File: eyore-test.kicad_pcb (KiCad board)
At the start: 2 copper layers, 50 x 50 mm, 29 parts, among them P1 USB_5PIN_SHELL, P2 CONN_01X04, P3 CONN_01X02, SW1 SW_PUSHBUTTON, SW2 SW_PUSHBUTTON, U1 LD1117S33CTR, U2 STM32F072C8, U3 ESP-12E, U4 ESP-12E

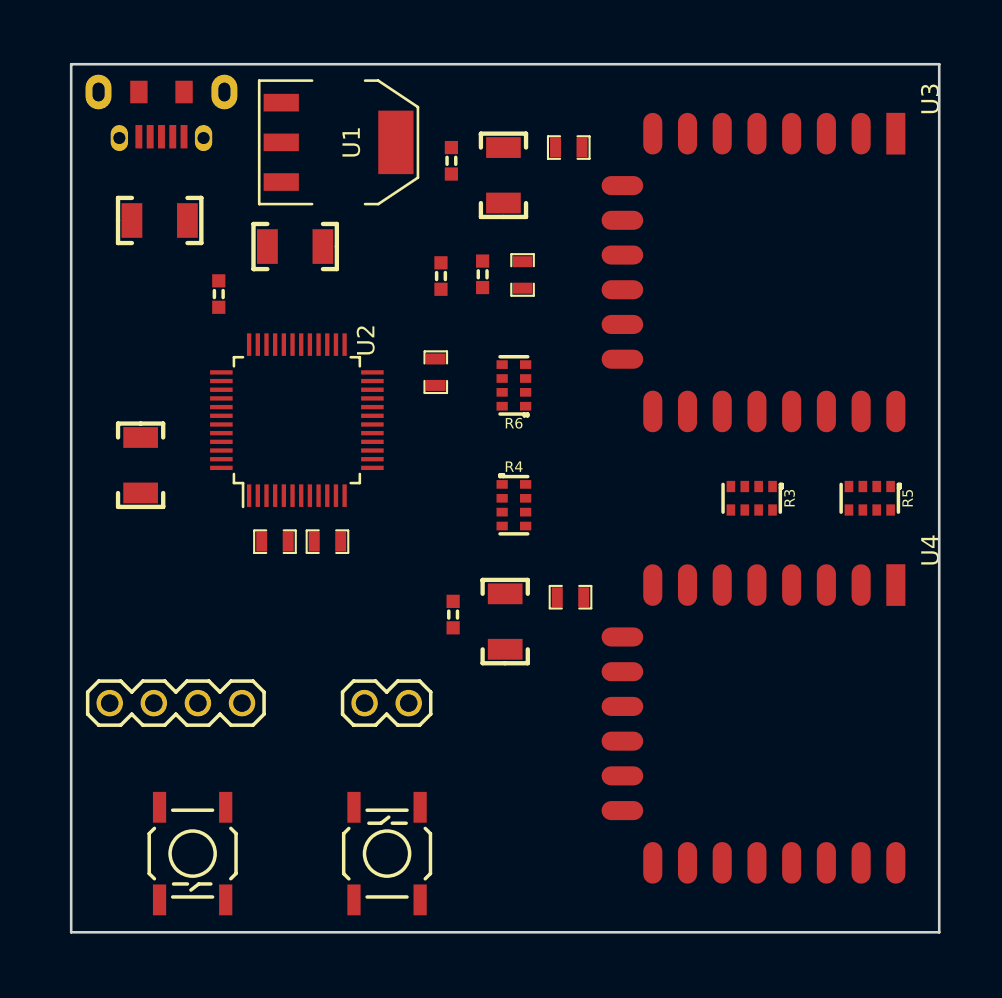
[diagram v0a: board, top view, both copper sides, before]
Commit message: Part routed, but I think approach was wrong
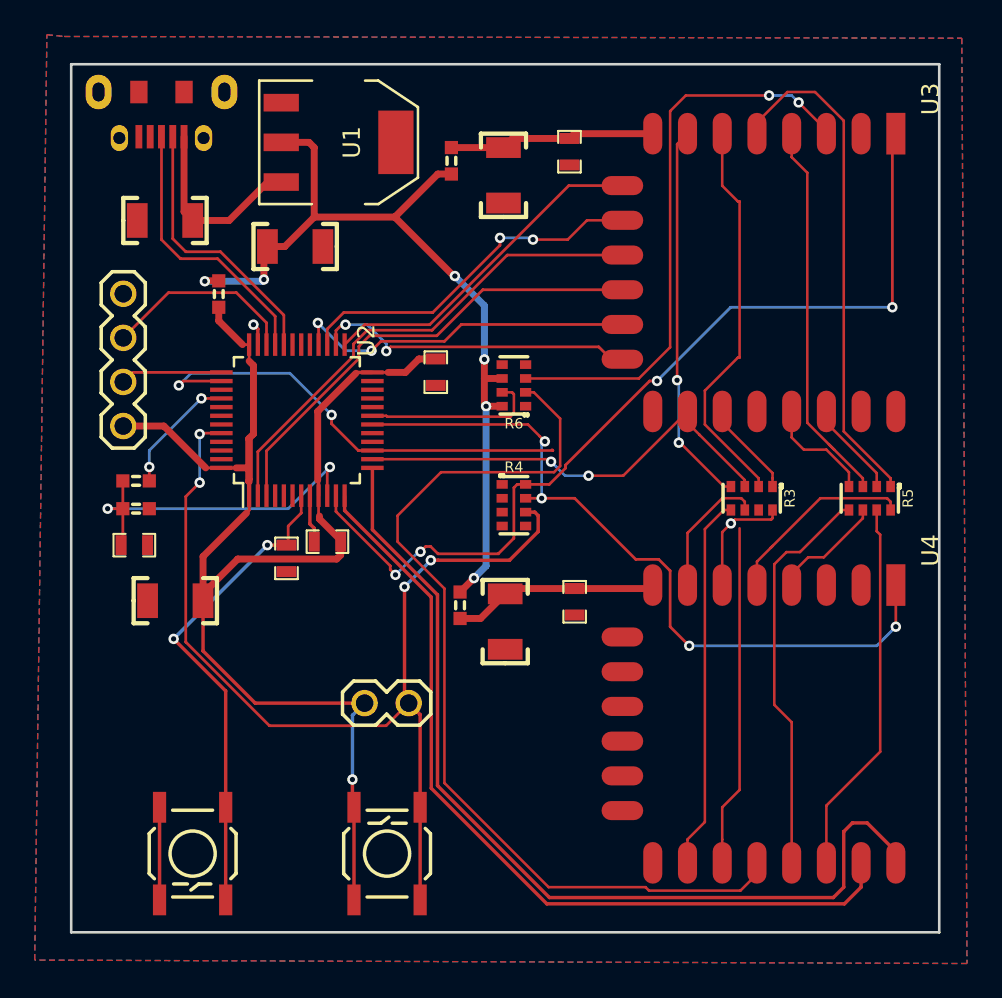
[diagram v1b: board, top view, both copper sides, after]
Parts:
- moved C4 27.2 mm to (116.6, 97.7), turned to 0 degrees
- moved R2 24.1 mm to (116.7, 95.6), turned to 180 degrees
- moved R1 21.2 mm to (116.7, 94.0), turned to 0 degrees
- moved P2 17.4 mm to (116.0, 90.8), turned to 90 degrees
- moved C5 8.05 mm to (119.0, 100.9), turned to 180 degrees
- moved C3 1.17 mm to (125.4, 98.5), turned to 270 degrees
- moved L3 0.67 mm to (135.4, 101.2), turned to 270 degrees
- moved C11 0.35 mm to (142.0, 101.0), turned to 270 degrees
- moved C1 0.30 mm to (118.4, 79.0)
- moved C10 0.24 mm to (141.7, 75.0), turned to 270 degrees
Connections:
- P2 pad 1: +3V3 -> /STM_VCC
- P3 pad 1: +3V3 -> /STM_VCC
- R3 pad 1: /A_GPIO16 -> /A_GPIO2
- R3 pad 2: /B_GPIO16 -> /B_GPIO2
- R3 pad 3: /A_GPIO14 -> /A_GPIO12
- R3 pad 4: /B_GPIO14 -> /B_GPIO12
- R3 pad 5: /A_GPIO12 -> /A_GPIO15
- R3 pad 6: /B_GPIO12 -> /B_GPIO13
- R3 pad 7: /A_GPIO2 -> /A_GPIO13
- R3 pad 8: /B_GPIO2 -> /B_GPIO15
- R5 pad 1: /A_GPIO13 -> /A_GPIO14
- R5 pad 2: /B_GPIO13 -> /B_GPIO14
- R5 pad 3: /A_GPIO15 -> /A_GPIO5_SDA
- R5 pad 4: /B_GPIO15 -> /B_GPIO5
- R5 pad 5: /A_GPIO5_SDA -> /A_GPIO16
- R5 pad 6: /B_GPIO5 -> /B_GPIO16
- SW1 pad 1: +3V3 -> /STM_VCC
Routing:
- net /STM_VCC: track 0.00 -> 85.7 mm, vias 0 -> 1
- net /STM_BOOT: track 0.00 -> 58.1 mm, vias 0 -> 4
- net /A_GPIO14: track 0.00 -> 55.9 mm, vias 0 -> 2
- net /B_GPIO0: track 0.00 -> 54.0 mm
- net /B_UART_TX: track 0.00 -> 53.9 mm
- net /A_~RST: track 0.00 -> 53.2 mm, vias 0 -> 4
- net +3V3: track 0.00 -> 51.1 mm, vias 0 -> 6
- net /B_UART_RX: track 0.00 -> 48.2 mm
- net /B_~RST: track 0.00 -> 43.3 mm, vias 0 -> 4
- net /A_ENABLE: track 0.00 -> 33.1 mm, vias 0 -> 2
- net /A_SPI_GPIO9: track 0.00 -> 28.6 mm
- net /STM_~RST: track 0.00 -> 28.0 mm, vias 0 -> 2
- net /A_SPI_GPIO10: track 0.00 -> 27.3 mm
- net /A_GPIO15: track 0.00 -> 25.8 mm, vias 0 -> 2
- net /B_GPIO4: track 0.00 -> 23.2 mm
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- added copper zone on B.Cu, net GND
- added copper zone on F.Cu, net GND
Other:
- net class Default: clearance 0.2 -> 0.15; trace_width 0.25 -> 0.15; via_drill 0.4 -> 0.3
- net class Power added: clearance 0.2, trace_width 0.25, via_dia 0.6, via_drill 0.3
- rule trace_clearance: 0.2 -> 0.15
- rule trace_min: 0.2 -> 0.15

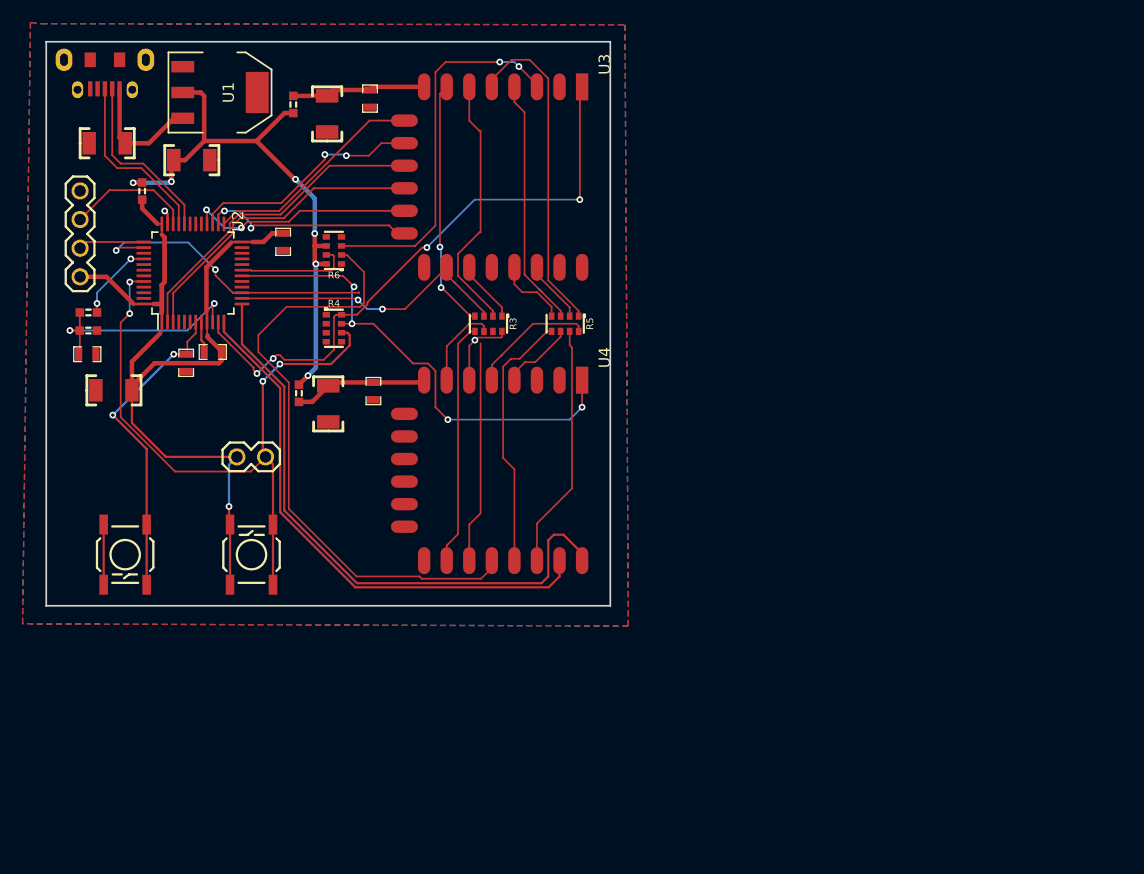
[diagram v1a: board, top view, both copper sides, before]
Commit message: Routed 4 layer version
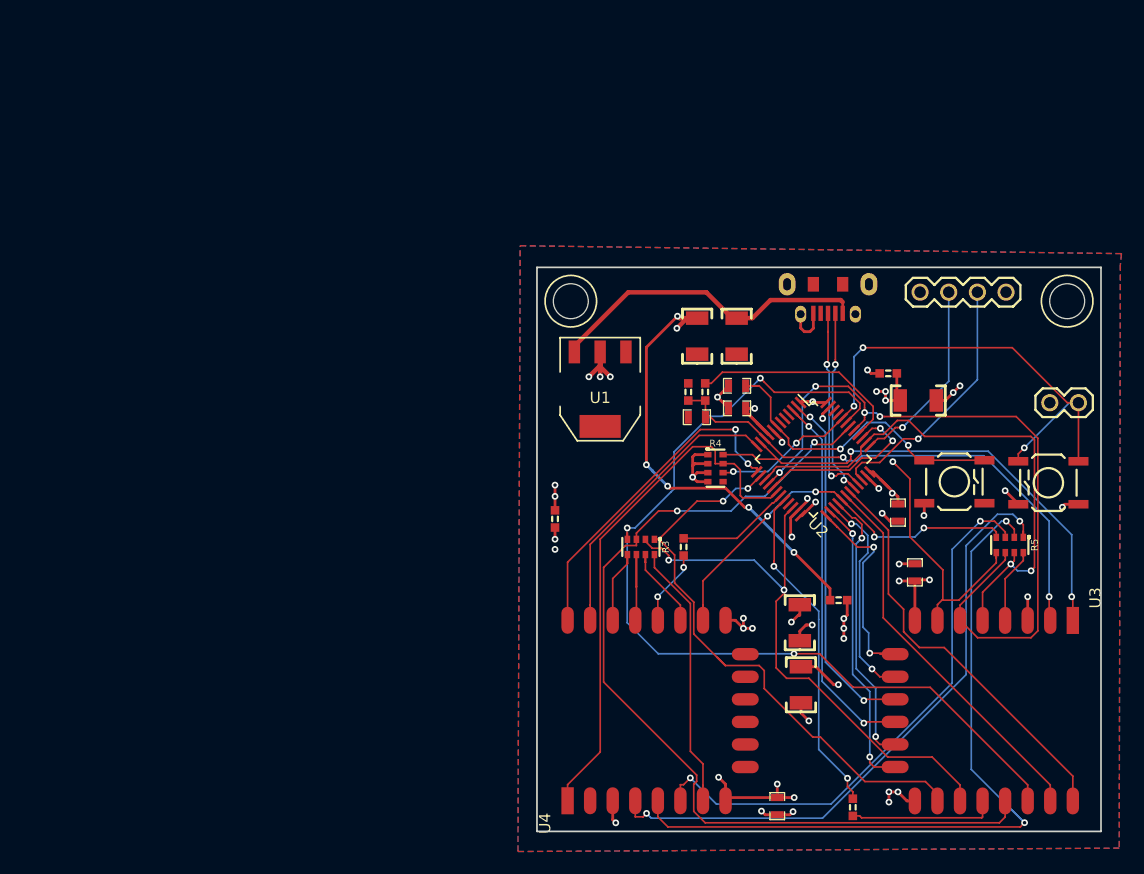
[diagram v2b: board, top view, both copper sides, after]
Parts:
- added 1pin: VAL**, Connect:1pin, F.Cu at (203.5, 93.0)
- added 1pin: VAL**, Connect:1pin, F.Cu at (159.5, 93.0)
- added R7: 10K, FT:0603, F.Cu at (184.5, 137.9)
- R6: value 220R -> 10K; footprint FT:RES_CAY16 -> FT:0603
- moved P2 74.5 mm to (190.5, 92.2), turned to 0 degrees
- moved SW2 73.8 mm to (193.5, 109.0), turned to 0 degrees
- moved P3 72.2 mm to (202.0, 102.0)
- moved C5 71.3 mm to (190.3, 101.8), turned to 0 degrees
- moved SW1 70.9 mm to (201.8, 109.1), turned to 180 degrees
- moved L1 68.1 mm to (187.6, 99.4), turned to 0 degrees
- moved P1 67.1 mm to (182.3, 94.1)
- moved C8 65.8 mm to (179.9, 127.0)
- moved L2 65.3 mm to (183.2, 119.5), turned to 0 degrees
- moved U3 64.3 mm to (204.0, 121.3)
- moved C10 64.0 mm to (190.0, 117.0), turned to 90 degrees
- moved C7 62.4 mm to (188.5, 111.7), turned to 270 degrees
- moved C1 58.4 mm to (174.2, 96.1), turned to 270 degrees
- moved U2 57.4 mm to (181.0, 107.0), turned to 315 degrees
- moved R1 55.1 mm to (171.4, 101.0), turned to 90 degrees
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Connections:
- R3 pad 1: /A_GPIO2 -> /A_GPIO15
- R3 pad 2: /B_GPIO2 -> /B_GPIO13
- R3 pad 3: /A_GPIO12 -> /A_GPIO2
- R3 pad 4: /B_GPIO12 -> /B_GPIO2
- R3 pad 5: /A_GPIO15 -> /A_GPIO4_SCL
- R3 pad 6: /B_GPIO13 -> /B_GPIO4
- R3 pad 7: /A_GPIO13 -> /A_GPIO5_SDA
- R3 pad 8: /B_GPIO15 -> /B_GPIO5
- R5 pad 1: /A_GPIO14 -> /B_GPIO16
- R5 pad 2: /B_GPIO14 -> /A_GPIO16
- R5 pad 3: /A_GPIO5_SDA -> /B_GPIO14
- R5 pad 4: /B_GPIO5 -> /A_GPIO14
- R5 pad 5: /A_GPIO16 -> /B_GPIO12
- R5 pad 6: /B_GPIO16 -> /A_GPIO12
- R5 pad 7: /A_GPIO4_SCL -> /B_GPIO15
- R5 pad 8: /B_GPIO4 -> /A_GPIO13
- R6 pad 1: /B_ENABLE -> /B_~FLASH
- R6 pad 2: +3V3 -> /B_GPIO0
- U3 pad 3: /A_ENABLE -> /A_VCC
- U4 pad 3: /B_ENABLE -> /B_VCC
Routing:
- net /A_GPIO5_SDA: track 6.48 -> 84.0 mm, vias 0 -> 3
- net /A_GPIO4_SCL: track 6.45 -> 83.8 mm, vias 0 -> 2
- net /B_GPIO14: track 11.3 -> 68.9 mm, vias 0 -> 2
- net /STM_VCC: track 85.7 -> 33.9 mm, vias 1 -> 9
- net /B_GPIO16: track 6.55 -> 56.0 mm, vias 0 -> 2
- net /B_GPIO0: track 54.0 -> 7.35 mm, vias 0 -> 2
- net /A_GPIO2: track 5.52 -> 51.6 mm, vias 0 -> 2
- net /B_GPIO12: track 4.29 -> 49.6 mm, vias 1 -> 2
- net /A_GPIO12: track 23.0 -> 67.3 mm, vias 0 -> 4
- net /A_UART_TX: track 0.00 -> 36.9 mm
- net GND: track 9.34 -> 43.9 mm, vias 1 -> 22
- net /A_UART_RX: track 0.00 -> 34.5 mm
- net /A_ENABLE: track 33.1 -> 0.00 mm, vias 2 -> 0
- net /A_~FLASH: track 0.00 -> 31.0 mm, vias 0 -> 2
- net /A_AIN: track 20.1 -> 46.5 mm
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- added copper zone on VCC, net +3V3
- added copper zone on VCC, net /A_VCC
- added copper zone on VCC, net /B_VCC
- added copper zone on VCC, net /STM_VCC
- added copper zone on Gnd, net GND
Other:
- copper layers 2 -> 4

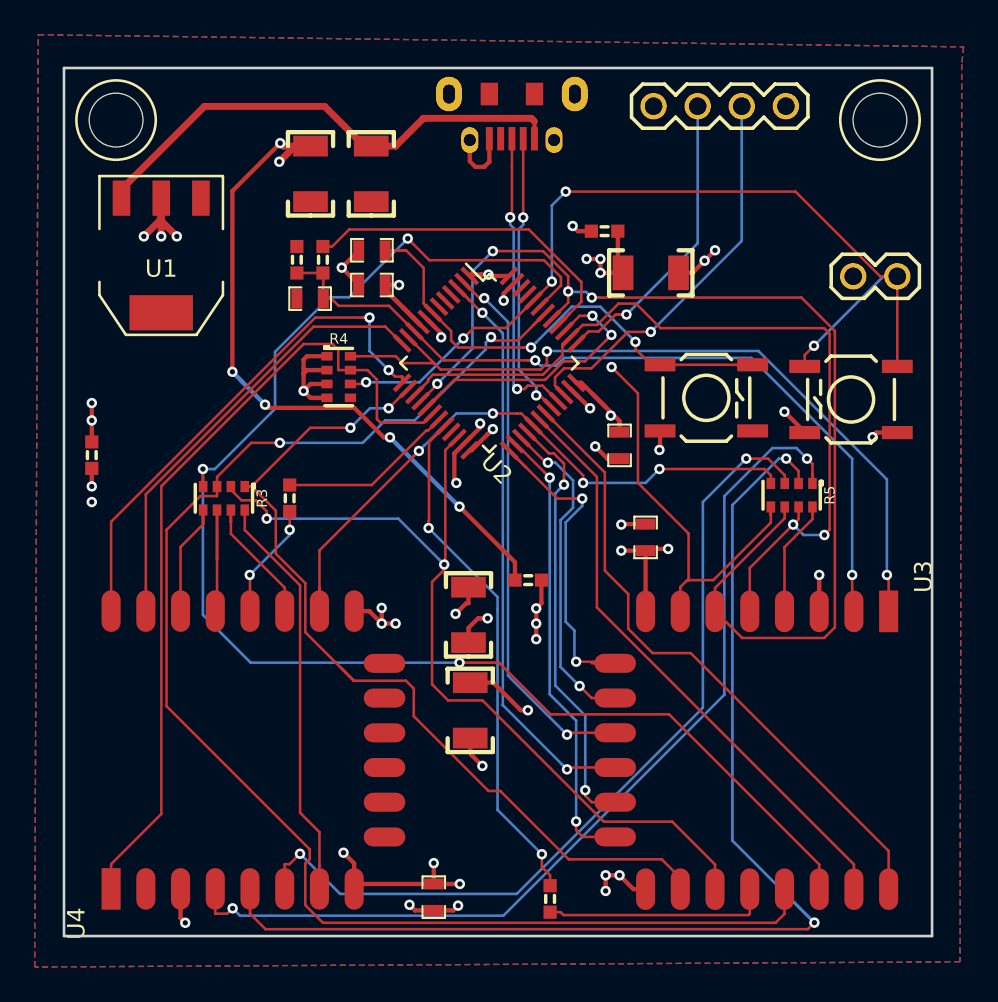
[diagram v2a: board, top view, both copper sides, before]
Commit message: Rerouted as 2 layers
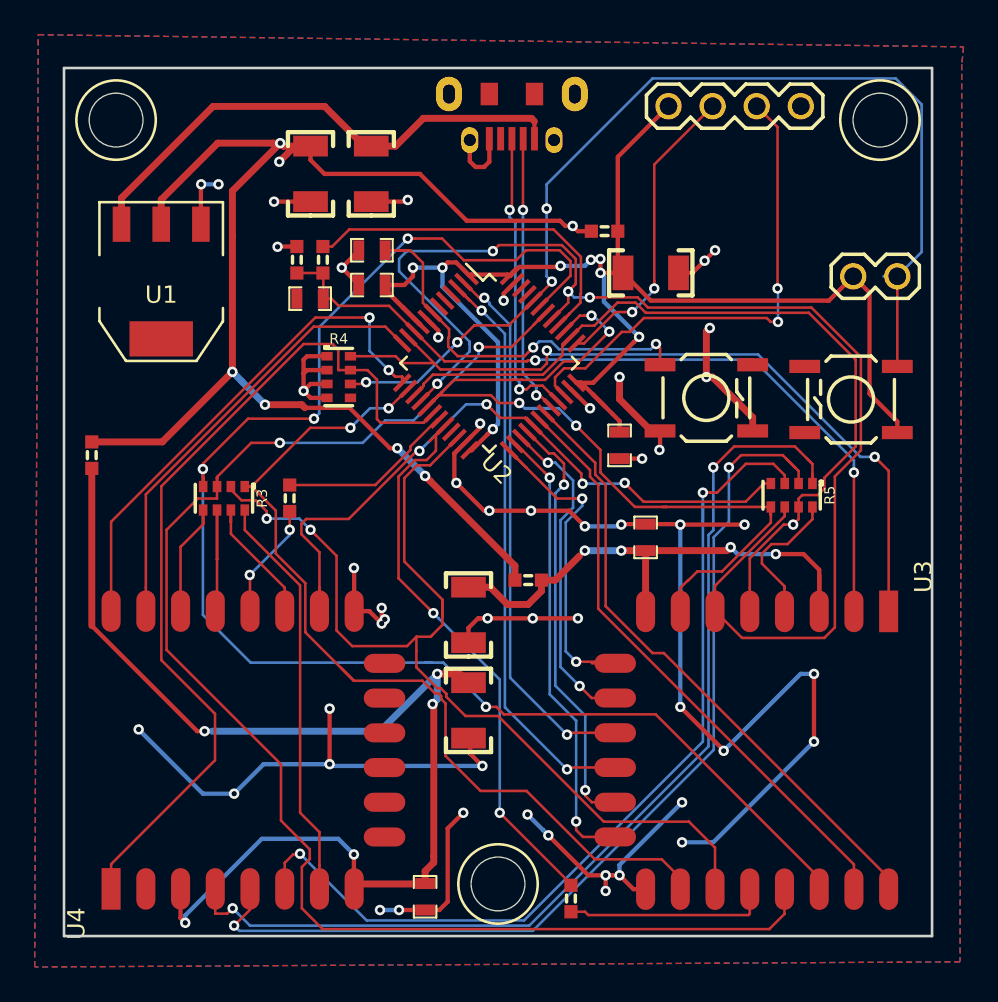
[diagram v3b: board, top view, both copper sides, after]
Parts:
- added 1pin: VAL**, Connect:1pin, F.Cu at (181.5, 137.0)
- moved C8 5.50 mm to (179.8, 121.5)
- moved C9 5.50 mm to (179.8, 127.0)
- moved U1 1.50 mm to (162.1, 102.3)
- moved R7 1.20 mm to (185.7, 137.8)
- moved P2 0.86 mm to (191.3, 92.2)
- moved C11 0.50 mm to (177.3, 137.7)
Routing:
- net GND: track 43.9 -> 165.8 mm, vias 22 -> 51
- net /STM_VCC: track 33.9 -> 94.0 mm, vias 9 -> 8
- net /B_VCC: track 15.7 -> 68.4 mm, vias 7 -> 5
- net +3V3: track 53.0 -> 80.1 mm, vias 12 -> 7
- net /A_VCC: track 15.8 -> 30.9 mm, vias 7 -> 4
- net /A_GPIO13: track 43.3 -> 55.8 mm, vias 3 -> 4
- net /B_GPIO14: track 68.9 -> 57.3 mm
- net /A_GPIO12: track 67.3 -> 76.4 mm
- net /A_GPIO2: track 51.6 -> 59.5 mm
- net /STM_BOOT: track 54.3 -> 60.9 mm, vias 5 -> 4
- net /STM_~RST: track 29.2 -> 23.7 mm
- net /SWDIO: track 23.0 -> 28.5 mm, vias 1 -> 2
- net /A_GPIO5_SDA: track 84.0 -> 88.0 mm, vias 3 -> 4
- net /B_GPIO12: track 49.6 -> 53.2 mm
- net /B_GPIO16: track 56.0 -> 59.6 mm
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- removed copper zone on VCC, net +3V3
- removed copper zone on VCC, net /A_VCC
- removed copper zone on VCC, net /B_VCC
- removed copper zone on VCC, net /STM_VCC
- removed copper zone on Gnd, net GND
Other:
- copper layers 4 -> 2
- rule trace_min: 0.15 -> 0

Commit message: Ready for V0.1 prototype
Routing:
- net /B_GPIO4: track 8.73 -> 5.87 mm
- net +5V: track 30.2 -> 29.0 mm
- net /B_GPIO2: track 7.80 -> 8.54 mm
- net GND: track 165.8 -> 166.4 mm
- net /B_GPIO13: track 23.8 -> 24.4 mm
- net /B_UART_TX: track 30.0 -> 29.5 mm
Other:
- rule pad_to_mask_clearance: 0.2 -> 0.1
- board text added: "1"
- board text added: "13"
- board text added: "25"
- board text added: "3.3V"
- board text added: "37"
- board text added: "ESP A"
- board text added: "ESP B"
- board text added: "GND"
- board text added: "STM BOOT0"
- board text added: "STM BOOT0 Jumper on"
- board text added: "STM DEBUG"
- board text added: "STM RESET"
- board text added: "SWCLK"
- board text added: "SWDIO"
- board text added: "V1.0"
- board text added: "by Angus Gratton TAPR OHL"
- board text added: "eyore-test"

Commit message: V1.0 as ordered
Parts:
- added TP1: TESTPOINT, FT:1X01, F.Cu at (202.4, 118.3)
- added TP2: TESTPOINT, FT:1X01, F.Cu at (183.4, 130.2)
- added TP3: TESTPOINT, FT:1X01, F.Cu at (158.6, 108.7)
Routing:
- net GND: track 166.4 -> 169.2 mm, vias 51 -> 52
- net /A_~FLASH: track 33.3 -> 32.1 mm
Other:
- rule pad_to_mask_clearance: 0.1 -> 0.15
- board text added: "TP-ADC"
- board text added: "TP-GPIO2"
- board text added: "github.com/projectgus/eyore-test"
